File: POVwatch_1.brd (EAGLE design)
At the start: 25.4 x 40 mm, 51 parts, among them Q1 S8050, U1 ATMEGA168P-QFN32, U2 ADXL345, U3 MCP6001-SOT23, U4 APDS-9008, U5 TP4055, U6 3.3V, U7 CH340E, Y1 7.3728MHz

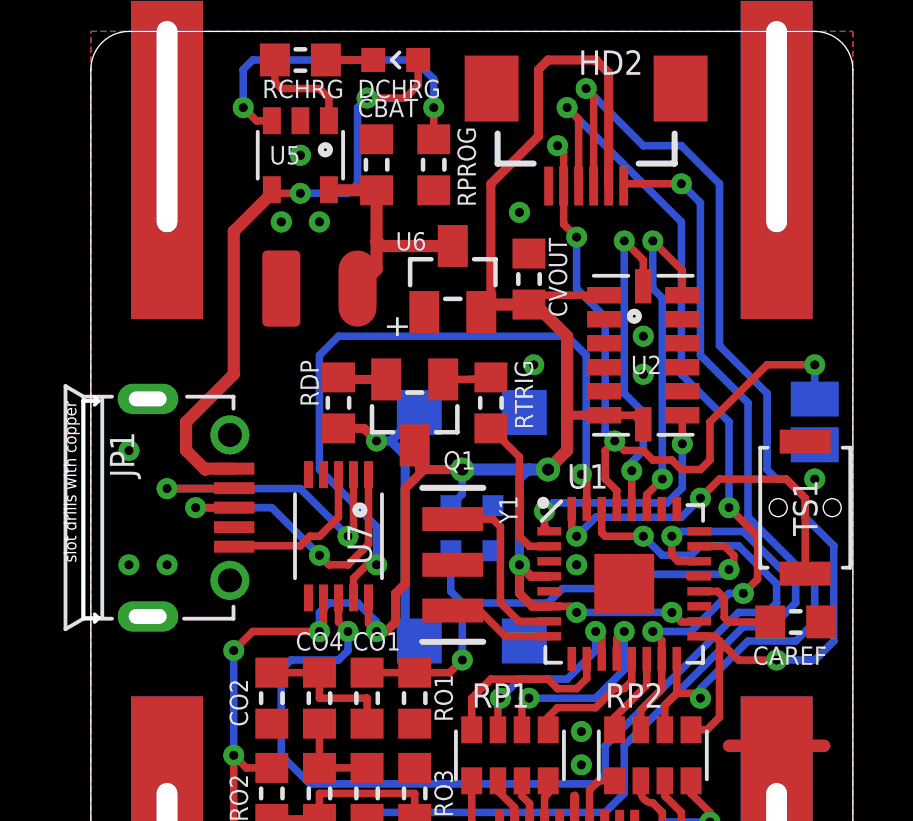
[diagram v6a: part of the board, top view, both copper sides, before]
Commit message: Fix the problem that mask always broken around the crystal
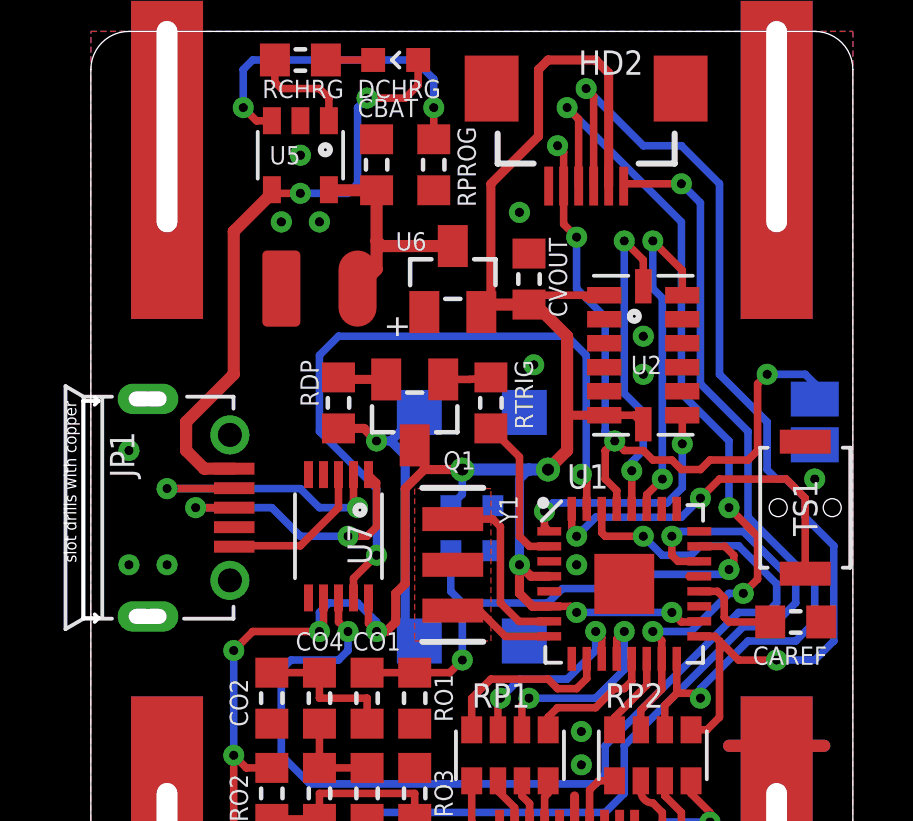
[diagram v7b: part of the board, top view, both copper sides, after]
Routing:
- net UD-: track 11.1 -> 10.0 mm
- net UD+: track 10.4 -> 9.70 mm

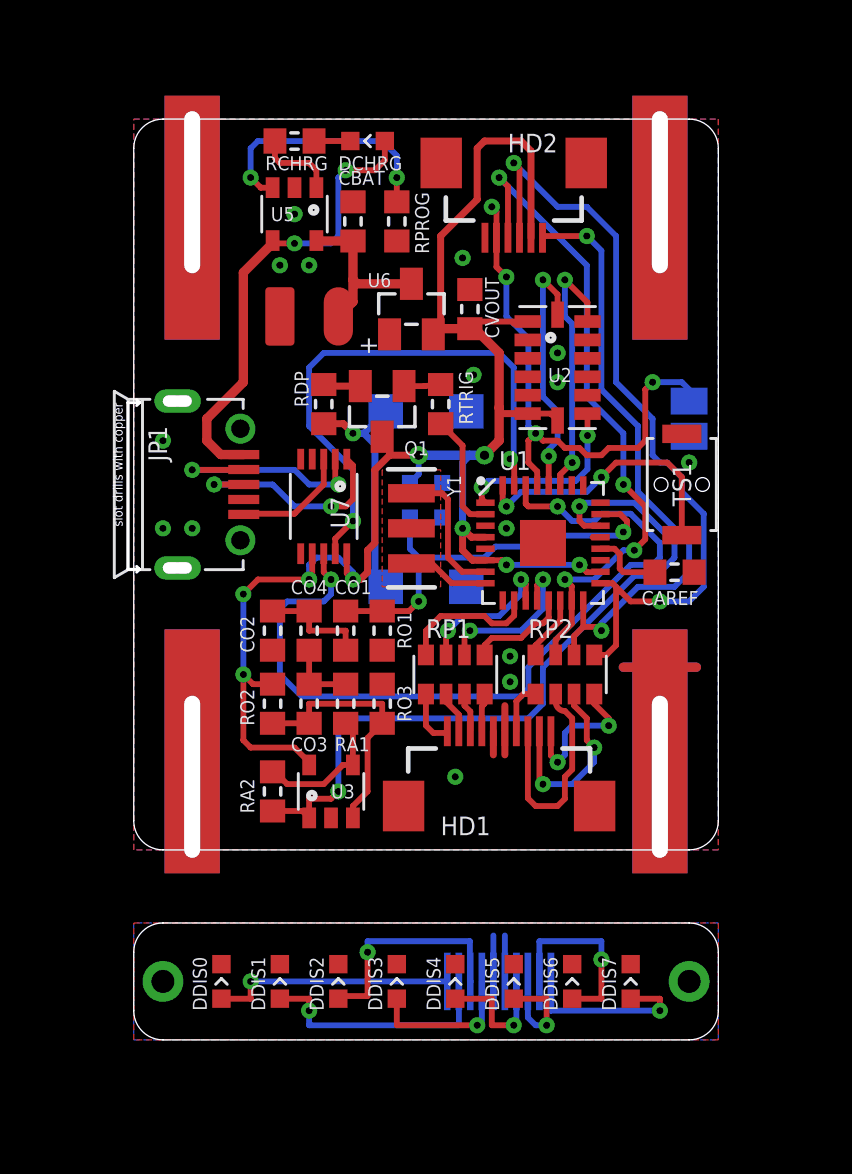
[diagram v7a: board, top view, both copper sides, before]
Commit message: Fixed CH340E ground connection
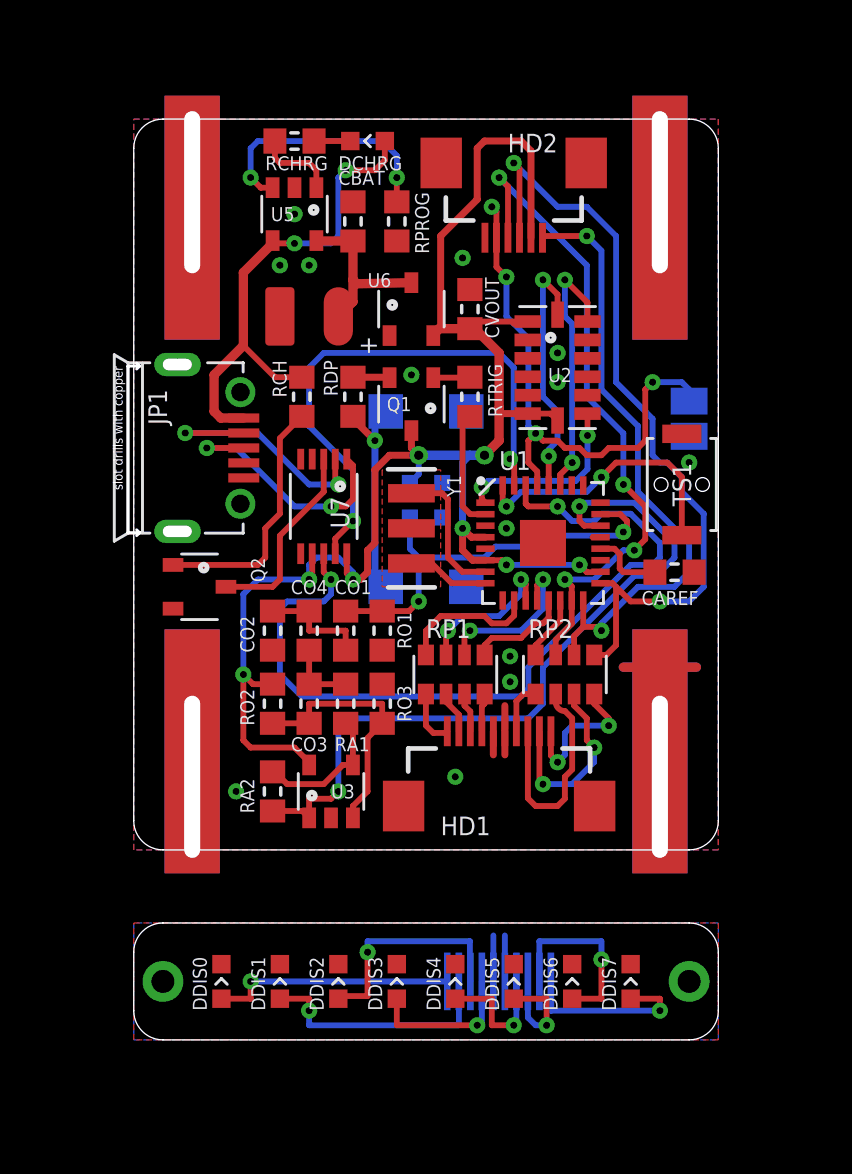
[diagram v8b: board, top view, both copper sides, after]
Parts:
- added Q2: S8050, MyLibrary:SOT23-0
- added RCH: 10kΩ, MyLibrary:SMD0603
- Q1, U6: device MyLibrary:SOT23 -> MyLibrary:SOT23-0
- moved JP1 1.59 mm to (1.91, 25.7)
- moved RDP 1.31 mm to (9.53, 27.9)
- moved RTRIG 1.31 mm to (14.6, 27.9)
- moved Q1 1.31 mm to (12.1, 27.6)
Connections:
- new net TRIGND: Q2.1, RCH.1
- net GND: now also JP1.5, Q2.2
- net GND(CH340E): now also Q2.3; no longer JP1.5
- net VUSB: now also RCH.2
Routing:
- net TRIGND: track 0.00 -> 10.9 mm
- net GND(CH340E): track 5.12 -> 8.49 mm
- net UD+: track 9.70 -> 11.0 mm
- net UD-: track 10.0 -> 11.3 mm
- net VUSB: track 20.5 -> 21.7 mm
- net RDP: track 10.3 -> 9.46 mm
- net VDD_3V3: track 74.5 -> 74.6 mm, vias 9 -> 8
- net GND: vias 15 -> 13
